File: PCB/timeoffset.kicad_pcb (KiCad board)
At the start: 2 copper layers, 15.2 x 23.7 mm, 8 parts

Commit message: ideas about adding reboot support
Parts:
- added C3: 0.01, Capacitor_SMD:C_0603_1608Metric, B.Cu at (128.7, 82.6)
- added D1: D, Diode_THT:D_5KP_P7.62mm_Vertical_AnodeUp, F.Cu at (115.8, 84.9)
- SPI_In1: renamed from SPI In
- moved C1 0.60 mm to (117.7, 89.1)
- moved C2 0.19 mm to (120.9, 89.5)
- renumbered Power to J1, IRF7204 to Q1, ATtiny13A-SU to U1
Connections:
- net Net-(C1-Pad2) renamed GND
- J1 pad 2: Net-(C1-Pad1) -> Net-(D1-Pad2)
- Q1 pad 1: Net-(C1-Pad1) -> Net-(D1-Pad2)
- R2 pad 2: Net-(C1-Pad1) -> Net-(D1-Pad2)
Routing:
- net Net-(C1-Pad1): track 52.2 -> 27.1 mm
- net Net-(D1-Pad2): track 0.00 -> 19.8 mm
- net GND: track 33.2 -> 35.5 mm, vias 0 -> 2
- net Net-(C3-Pad1): track 13.5 -> 14.8 mm

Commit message: update
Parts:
- turned R1 to 90 degrees
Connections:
- R1 pad 1: Net-(C1-Pad1) -> Net-(D1-Pad2)
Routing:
- net Net-(D1-Pad2): track 19.8 -> 34.6 mm, vias 0 -> 2
- net Net-(C1-Pad1): track 27.1 -> 24.6 mm
- net Net-(C3-Pad1): track 14.8 -> 13.5 mm

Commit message: Update, will finally try it very soon, I hope
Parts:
- D1: footprint Diode_THT:D_5KP_P7.62mm_Vertical_AnodeUp -> Diode_SMD:D_SMB; moved to B.Cu
- moved D1 2.32 mm to (115.8, 82.6)
- moved R1 0.49 mm to (128.7, 89.8)
- moved C1 0.47 mm to (118.1, 89.1)
- moved U1 0.41 mm to (124.9, 89.6)
- moved C2 0.39 mm to (121.2, 89.6)
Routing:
- net Net-(D1-Pad2): track 34.6 -> 43.0 mm
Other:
- board size 15.2 x 23.7 mm -> 15.3 x 23.8 mm
- net class Default removed
- rule pad_to_mask_clearance: 0.051 -> 0

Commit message: Smaller form
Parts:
- added J2: Conn_01x03, Connector_JST:JST_PH_S3B-PH-K_1x03_P2.00mm_Horizontal, F.Cu at (117.2, 87.1)
- D1: footprint Diode_SMD:D_SMB -> Diode_SMD:D_SMA
- moved C2 3.22 mm to (121.7, 92.8)
- moved D1 2.89 mm to (118.6, 82.3), turned to 90 degrees
- moved C1 2.01 mm to (120.1, 89.0)
- moved R2 1.42 mm to (128.6, 98.5)
- moved Q1 1.10 mm to (124.1, 98.8)
- moved J1 0.74 mm to (117.8, 95.3)
- moved U1 0.45 mm to (125.4, 89.6)
- moved R1 0.13 mm to (128.8, 89.8)
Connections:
- D1 pad 2: Net-(D1-Pad2) -> Net-(J1-Pad2)
- J1 pad 2: Net-(D1-Pad2) -> Net-(J1-Pad2)
- Q1 pad 1: Net-(D1-Pad2) -> Net-(Q1-Pad1)
- R1 pad 1: Net-(D1-Pad2) -> Net-(J1-Pad2)
- R2 pad 2: Net-(D1-Pad2) -> Net-(Q1-Pad1)
- SPI_In1 pad 2: Net-(C1-Pad1) -> Net-(J1-Pad2)
- U1 pad 3: Net-(U1-Pad3) -> unconnected-(U1-Pad3)
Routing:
- net Net-(D1-Pad2): track 43.0 -> 0.00 mm, vias 2 -> 0
- net Net-(J1-Pad2): track 0.00 -> 39.0 mm, vias 0 -> 2
- net Net-(Q1-Pad1): track 0.00 -> 10.7 mm, vias 0 -> 1
- net Net-(C1-Pad1): track 24.9 -> 20.9 mm
- net GND: track 35.9 -> 32.3 mm
- net Net-(SPI_In1-Pad4): track 11.2 -> 10.7 mm
- removed copper zone on B.Cu, net (none)
- removed copper zone on B.Cu, net GND
- removed copper zone on F.Cu, net GND
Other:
- board size 15.3 x 23.8 mm -> 14.3 x 23.9 mm

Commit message: board optimization
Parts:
- removed J2: Conn_01x03, Connector_JST:JST_PH_S3B-PH-K_1x03_P2.00mm_Horizontal
- moved C1 2.05 mm to (118.1, 89.1)
- moved D1 0.53 mm to (118.1, 82.2)
- moved J1 0.50 mm to (117.3, 95.3)
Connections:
- Q1 pad 1: Net-(Q1-Pad1) -> Net-(C1-Pad1)
- R2 pad 2: Net-(Q1-Pad1) -> Net-(C1-Pad1)
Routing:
- net Net-(C1-Pad1): track 20.9 -> 36.9 mm, vias 0 -> 2
- net Net-(D1-Pad2): track 39.0 -> 52.7 mm
- net Net-(Q1-Pad1): track 10.7 -> 0.00 mm, vias 1 -> 0
- net GND: track 32.3 -> 33.0 mm
- net Net-(J1-Pad3): track 8.60 -> 9.10 mm
- added copper zone on B.Cu, net GND
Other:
- board size 14.3 x 23.9 mm -> 15.1 x 23.9 mm

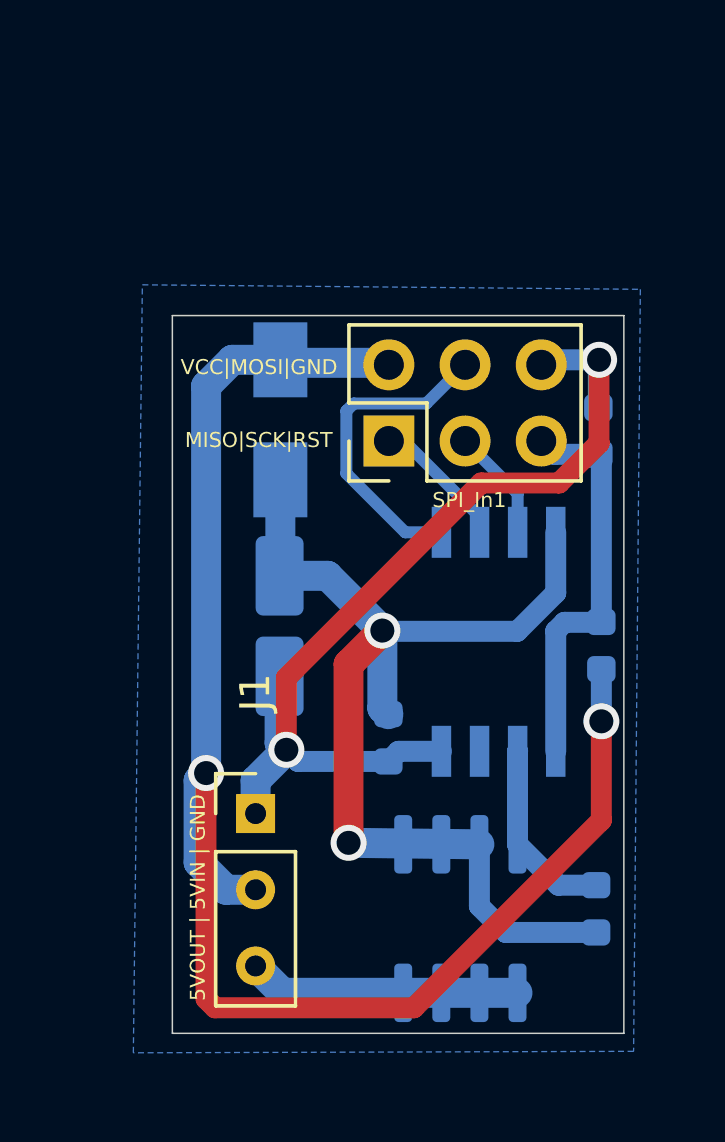
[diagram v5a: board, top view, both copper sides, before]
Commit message: horizontal connectors added
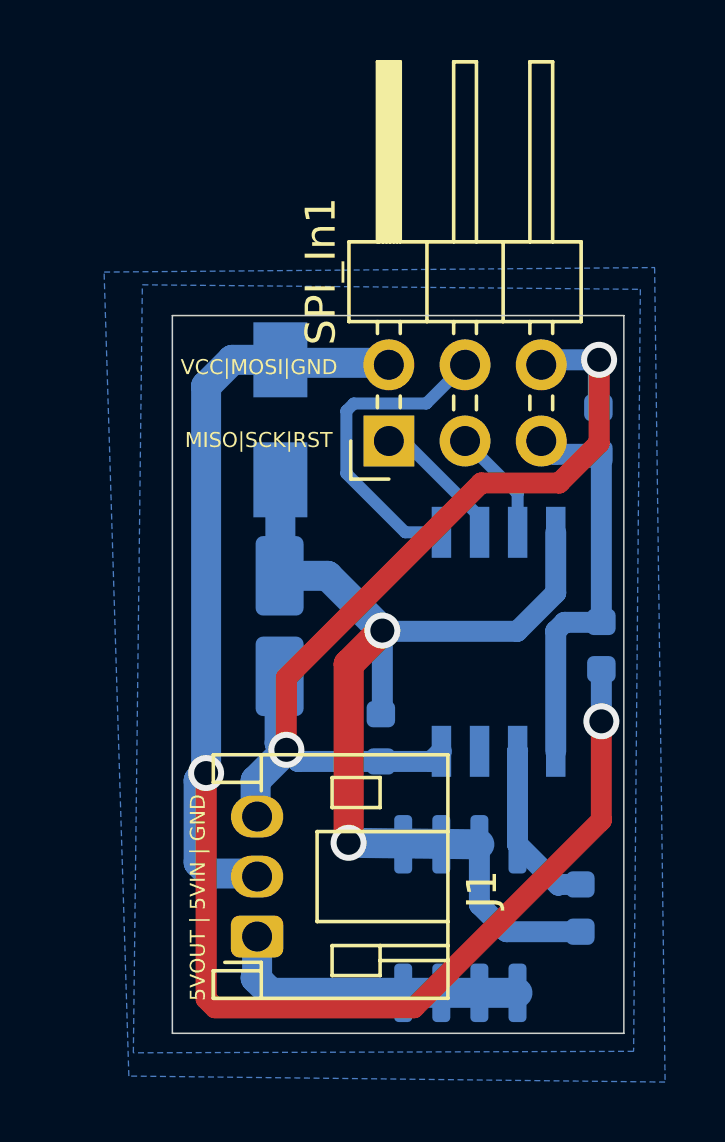
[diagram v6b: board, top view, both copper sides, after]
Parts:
- J1: footprint Connector_PinHeader_2.54mm:PinHeader_1x03_P2.54mm_Vertical -> Connector_JST:JST_PH_S3B-PH-K_1x03_P2.00mm_Horizontal
- SPI_In1: footprint Connector_PinHeader_2.54mm:PinHeader_2x03_P2.54mm_Vertical -> Connector_PinHeader_2.54mm:PinHeader_2x03_P2.54mm_Horizontal
- moved J1 4.10 mm to (117.3, 99.5), turned to 90 degrees
- moved R2 0.53 mm to (128.1, 98.5)
- moved C2 0.25 mm to (121.5, 92.8)
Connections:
- J1 pad 1: GND -> Net-(J1-Pad1)
- J1 pad 3: Net-(J1-Pad3) -> GND
- Q1 pad 3: Net-(J1-Pad3) -> Net-(J1-Pad1)
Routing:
- net Net-(J1-Pad1): track 0.00 -> 10.3 mm
- net Net-(J1-Pad3): track 9.10 -> 0.00 mm
- net Net-(C1-Pad1): track 36.9 -> 36.2 mm
- net Net-(Q1-Pad2): track 6.29 -> 5.77 mm
- added copper zone on B.Cu, net (none)

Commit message: Reset fix
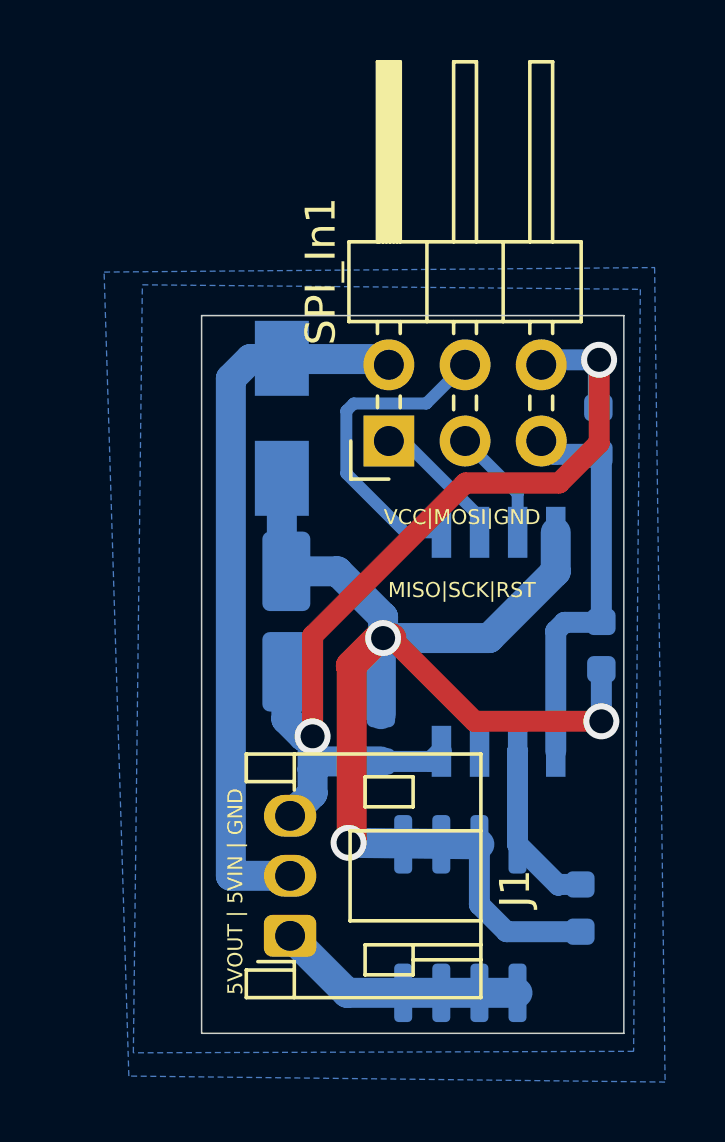
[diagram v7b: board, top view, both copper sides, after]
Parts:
- moved J1 1.10 mm to (118.4, 99.4)
- moved C1 0.27 mm to (118.3, 89.0)
- moved D1 0.07 mm to (118.2, 82.2)
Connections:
- R1 pad 1: Net-(D1-Pad2) -> Net-(C1-Pad1)
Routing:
- net Net-(D1-Pad2): track 52.5 -> 24.2 mm, vias 2 -> 0
- net Net-(C1-Pad1): track 36.2 -> 46.1 mm, vias 2 -> 3
- net Net-(J1-Pad1): track 10.3 -> 8.37 mm
- net GND: track 33.1 -> 32.1 mm
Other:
- board size 15.1 x 23.9 mm -> 14.1 x 23.9 mm
